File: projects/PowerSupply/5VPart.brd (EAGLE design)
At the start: 50 x 50 mm, 26 parts, among them IC1 LM2596T, IC2 LM2596T, X1 IN, X2 OUT

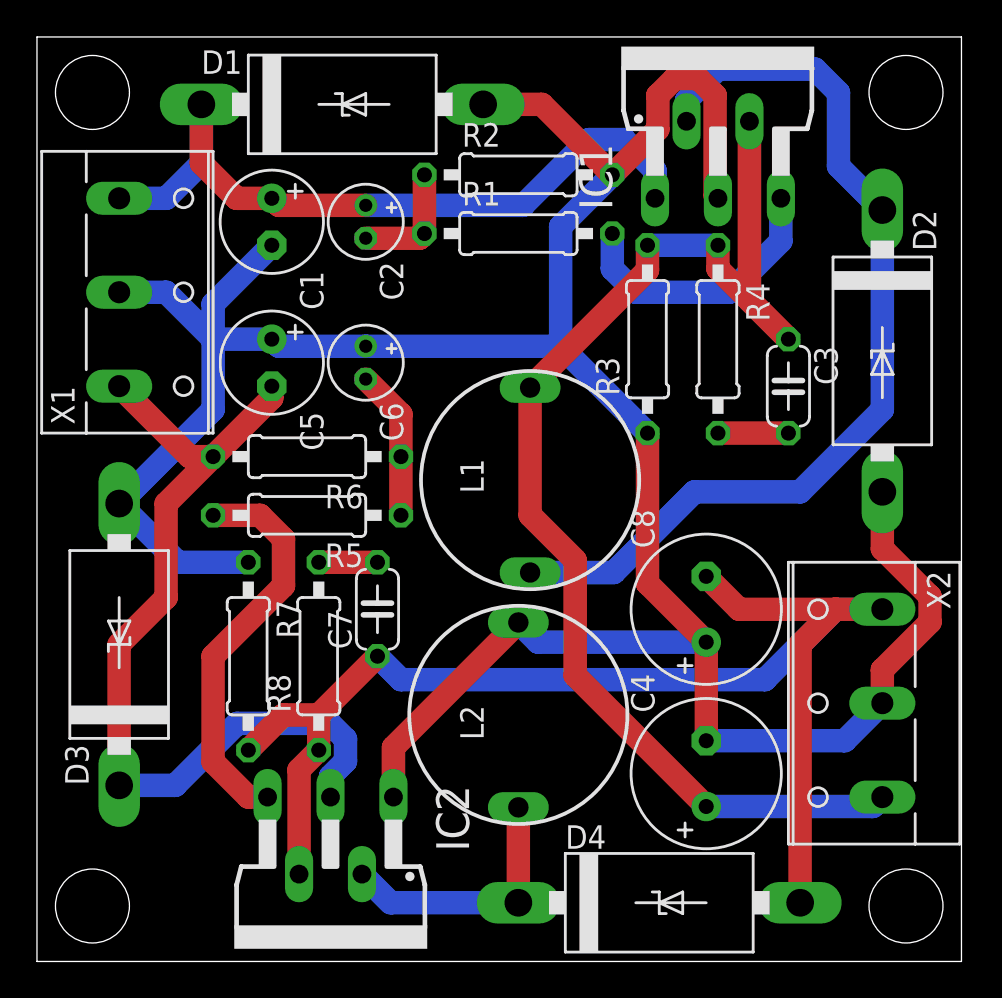
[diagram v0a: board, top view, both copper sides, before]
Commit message: feat: 5v part modified
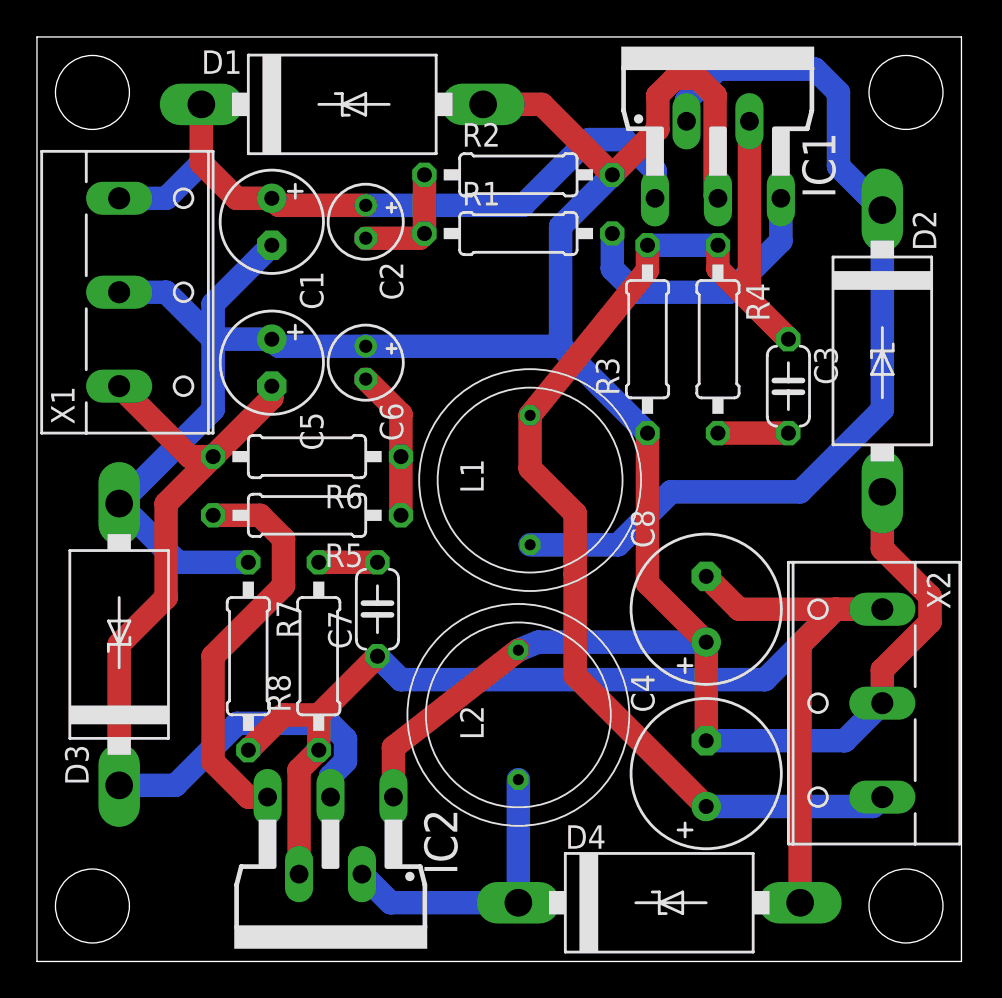
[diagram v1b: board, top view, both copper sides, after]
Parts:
- C8: value 330µF -> 470µF
- L1: device inductor-neosid:SD12-680 -> bb84:IND-120
- L2: value 47µH -> 33µH; device inductor-neosid:SD12-680 -> bb84:IND-120
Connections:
- net +5V: now also L1.P$2; no longer L1.2
- net GND: now also L2.P$2; no longer L2.2
- net N$2: now also L2.P$1; no longer L2.1
- net N$3: now also L1.P$1; no longer L1.1
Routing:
- net N$2: track 14.3 -> 15.8 mm
- net GND: track 155.9 -> 154.6 mm
- net +20V: track 41.4 -> 40.7 mm
- net N$3: track 51.4 -> 50.8 mm
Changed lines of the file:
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@@
 <attribute name="VALUE" x="21.082" y="16.891" size="1.27" layer="27" ratio="10" rot="R90"/>
 </element>
-<element name="C8" library="rcl" library_urn="urn:adsk.eagle:library:334" package="E3,5-8" package3d_urn="urn:adsk.eagle:package:23360/2" value="330µF" x="36.195" y="19.05" smashed="yes" rot="R90">
+<element name="C8" library="rcl" library_urn="urn:adsk.eagle:library:334" package="E3,5-8" package3d_urn="urn:adsk.eagle:package:23360/2" value="470µF" x="36.195" y="19.05" smashed="yes" rot="R90">
 <attribute name="NAME" x="33.401" y="22.352" size="1.27" layer="25" ratio="10" rot="R90"/>
 <attribute name="POPULARITY" value="13" x="66.675" y="49.53" size="1.778" layer="27" rot="R90" display="off"/>
@@
 <attribute name="MF" value="" x="83.82" y="38.735" size="1.778" layer="27" display="off"/>
 <attribute name="MPN" value="LM2596T-ADJ/LF02" x="83.82" y="38.735" size="1.778" layer="27" display="off"/>
-<attribute name="NAME" x="31.115" y="40.64" size="1.778" layer="25" ratio="10" rot="R90"/>
+<attribute name="NAME" x="43.18" y="41.275" size="1.778" layer="25" ratio="10" rot="R90"/>
 <attribute name="OC_FARNELL" value="9494162" x="83.82" y="38.735" size="1.778" layer="27" display="off"/>
 <attribute name="OC_NEWARK" value="65K5910" x="83.82" y="38.735" size="1.778" layer="27" display="off"/>
@@
 <attribute name="MF" value="" x="-5.715" y="24.13" size="1.778" layer="27" rot="R180" display="off"/>
 <attribute name="MPN" value="LM2596T-ADJ/LF02" x="-5.715" y="24.13" size="1.778" layer="27" rot="R180" display="off"/>
-<attribute name="NAME" x="21.59" y="9.525" size="1.778" layer="25" ratio="10" rot="R270"/>
+<attribute name="NAME" x="20.955" y="8.255" size="1.778" layer="25" ratio="10" rot="R270"/>
 <attribute name="OC_FARNELL" value="9494162" x="-5.715" y="24.13" size="1.778" layer="27" rot="R180" display="off"/>
 <attribute name="OC_NEWARK" value="65K5910" x="-5.715" y="24.13" size="1.778" layer="27" rot="R180" display="off"/>
@@
 <attribute name="VALUE" x="1.27" y="5.715" size="1.778" layer="27" ratio="10"/>
 </element>
-<element name="L1" library="inductor-neosid" library_urn="urn:adsk.eagle:library:241" package="SD12-680" package3d_urn="urn:adsk.eagle:package:14657/1" value="33µH" x="26.67" y="26.035" smashed="yes" rot="R90">
-<attribute name="MF" value="BUSSMANN" x="33.02" y="45.085" size="1.778" layer="27" rot="R90" display="off"/>
-<attribute name="MPN" value="SD12-680" x="33.02" y="45.085" size="1.778" layer="27" rot="R90" display="off"/>
+<element name="L1" library="bb84" package="IND-120" value="33µH" x="26.67" y="26.035" smashed="yes" rot="R90">
 <attribute name="NAME" x="24.162" y="25.317" size="1.27" layer="25" rot="R90"/>
-<attribute name="OC_FARNELL" value="unknown" x="33.02" y="45.085" size="1.778" layer="27" rot="R90" display="off"/>
-<attribute name="OC_NEWARK" value="19K7201" x="33.02" y="45.085" size="1.778" layer="27" rot="R90" display="off"/>
-<attribute name="POPULARITY" value="0" x="33.02" y="45.085" size="1.778" layer="27" rot="R90" display="off"/>
 <attribute name="VALUE" x="29.67" y="23.42" size="1.27" layer="27" rot="R90"/>
 </element>
-<element name="L2" library="inductor-neosid" library_urn="urn:adsk.eagle:library:241" package="SD12-680" package3d_urn="urn:adsk.eagle:package:14657/1" value="47µH" x="26.035" y="13.335" smashed="yes" rot="R90">
-<attribute name="MF" value="BUSSMANN" x="32.385" y="45.085" size="1.778" layer="27" rot="R90" display="off"/>
-<attribute name="MPN" value="SD12-680" x="32.385" y="45.085" size="1.778" layer="27" rot="R90" display="off"/>
+<element name="L2" library="bb84" package="IND-120" value="33µH" x="26.035" y="13.335" smashed="yes" rot="R90">
 <attribute name="NAME" x="24.162" y="11.982" size="1.27" layer="25" rot="R90"/>
-<attribute name="OC_FARNELL" value="unknown" x="32.385" y="45.085" size="1.778" layer="27" rot="R90" display="off"/>
-<attribute name="OC_NEWARK" value="19K7201" x="32.385" y="45.085" size="1.778" layer="27" rot="R90" display="off"/>
-<attribute name="POPULARITY" value="0" x="32.385" y="45.085" size="1.778" layer="27" rot="R90" display="off"/>
 <attribute name="VALUE" x="29.035" y="10.72" size="1.27" layer="27" rot="R90"/>
 </element>
@@
 <contactref element="R3" pad="1"/>
 <contactref element="D2" pad="A"/>
-<contactref element="L2" pad="2"/>
+<contactref element="L2" pad="P$2"/>
 <contactref element="R7" pad="1"/>
 <contactref element="C8" pad="+"/>
@@
 <contactref element="X1" pad="2"/>
 <wire x1="19.2786" y1="8.89" x2="19.2786" y2="11.5786" width="1.27" layer="1"/>
-<wire x1="19.2786" y1="11.5786" x2="26.035" y2="18.335" width="1.27" layer="1"/>
+<wire x1="19.2786" y1="11.5786" x2="26.035" y2="16.835" width="1.27" layer="1"/>
 <wire x1="36.195" y1="11.938" x2="36.195" y2="17.272" width="1.27" layer="1"/>
 <wire x1="36.195" y1="17.272" x2="33.02" y2="20.447" width="1.27" layer="1"/>
@@
 <wire x1="43.688" y1="11.938" x2="45.72" y2="13.97" width="1.27" layer="16"/>
 <wire x1="36.195" y1="17.272" x2="27.098" y2="17.272" width="1.27" layer="16"/>
-<wire x1="27.098" y1="17.272" x2="26.035" y2="18.335" width="1.27" layer="16"/>
+<wire x1="27.098" y1="17.272" x2="26.035" y2="16.835" width="1.27" layer="16"/>
 <wire x1="17.78" y1="33.274" x2="28.321" y2="33.274" width="1.27" layer="16"/>
 <wire x1="28.321" y1="33.274" x2="33.02" y2="28.575" width="1.27" layer="16"/>
@@
 <contactref element="IC1" pad="2"/>
 <contactref element="D2" pad="C"/>
-<contactref element="L1" pad="1"/>
-<wire x1="26.67" y1="21.035" x2="31.195" y2="21.035" width="1.27" layer="16"/>
-<wire x1="31.195" y1="21.035" x2="35.56" y2="25.4" width="1.27" layer="16"/>
-<wire x1="35.56" y1="25.4" x2="41.275" y2="25.4" width="1.27" layer="16"/>
-<wire x1="41.275" y1="25.4" x2="45.72" y2="29.845" width="1.27" layer="16"/>
+<contactref element="L1" pad="P$1"/>
+<wire x1="45.72" y1="29.845" x2="41.275" y2="25.4" width="1.27" layer="16"/>
 <wire x1="45.72" y1="29.845" x2="45.72" y2="40.64" width="1.27" layer="16"/>
 <wire x1="45.72" y1="40.64" x2="43.349" y2="43.011" width="1.27" layer="16"/>
@@
 <wire x1="36.83" y1="48.26" x2="35.1282" y2="46.5582" width="1.27" layer="16"/>
 <wire x1="35.1282" y1="46.5582" x2="35.1282" y2="45.4406" width="1.27" layer="16"/>
+<wire x1="31.425" y1="22.535" x2="26.67" y2="22.535" width="1.27" layer="16"/>
+<wire x1="41.275" y1="25.4" x2="34.29" y2="25.4" width="1.27" layer="16"/>
+<wire x1="34.29" y1="25.4" x2="31.425" y2="22.535" width="1.27" layer="16"/>
 </signal>
 <signal name="N$2">
-<contactref element="L2" pad="1"/>
+<contactref element="L2" pad="P$1"/>
 <contactref element="IC2" pad="2"/>
 <contactref element="D4" pad="C"/>
-<wire x1="26.035" y1="3.175" x2="26.035" y2="8.335" width="1.27" layer="1"/>
 <wire x1="26.035" y1="3.175" x2="19.1262" y2="3.175" width="1.27" layer="16"/>
 <wire x1="19.1262" y1="3.175" x2="17.5768" y2="4.7244" width="1.27" layer="16"/>
+<wire x1="26.035" y1="3.175" x2="26.035" y2="9.835" width="1.27" layer="16"/>
 </signal>
 <signal name="N$5">
@@
 <contactref element="R4" pad="1"/>
 <contactref element="C3" pad="1"/>
-<contactref element="L1" pad="2"/>
+<contactref element="L1" pad="P$2"/>
 <contactref element="C4" pad="+"/>
 <wire x1="40.64" y1="33.655" x2="36.83" y2="37.465" width="1.27" layer="1"/>
@@
 <wire x1="38.5318" y1="35.7632" x2="40.64" y2="33.655" width="1.27" layer="1"/>
 <wire x1="33.02" y1="38.735" x2="33.02" y2="37.385" width="1.27" layer="1"/>
-<wire x1="33.02" y1="37.385" x2="26.67" y2="31.035" width="1.27" layer="1"/>
-<wire x1="26.67" y1="31.035" x2="26.67" y2="24.14028125" width="1.27" layer="1"/>
-<wire x1="26.67" y1="24.14028125" x2="29.1074" y2="21.70288125" width="1.27" layer="1"/>
+<wire x1="33.02" y1="37.385" x2="26.67" y2="29.535" width="1.27" layer="1"/>
 <wire x1="29.1074" y1="15.4696" x2="36.195" y2="8.382" width="1.27" layer="1"/>
-<wire x1="29.1074" y1="21.70288125" x2="29.1074" y2="15.4696" width="1.27" layer="1"/>
+<wire x1="29.1074" y1="21.70288125" x2="29.1074" y2="20.955" width="1.27" layer="1"/>
+<wire x1="29.1074" y1="20.955" x2="29.1074" y2="15.4696" width="1.27" layer="1"/>
 <wire x1="33.02" y1="38.735" x2="36.83" y2="38.735" width="1.27" layer="16"/>
 <contactref element="X2" pad="1"/>
 <wire x1="45.72" y1="8.89" x2="45.212" y2="8.382" width="1.27" layer="16"/>
 <wire x1="45.212" y1="8.382" x2="36.195" y2="8.382" width="1.27" layer="16"/>
+<wire x1="26.67" y1="29.535" x2="26.67" y2="26.67" width="1.27" layer="1"/>
+<wire x1="29.1074" y1="24.2326" x2="29.1074" y2="21.70288125" width="1.27" layer="1"/>
+<wire x1="26.67" y1="26.67" x2="29.1074" y2="24.2326" width="1.27" layer="1"/>
 </signal>
 <signal name="-5V">
@@
 <contactref element="C2" pad="+"/>
 <contactref element="D1" pad="C"/>
-<wire x1="8.89" y1="45.72" x2="8.89" y2="46.355" width="1.27" layer="1"/>
-<wire x1="8.89" y1="43.18" x2="10.795" y2="41.275" width="1.27" layer="1"/>
+<wire x1="10.795" y1="41.275" x2="8.89" y2="43.18" width="1.27" layer="1"/>
 <wire x1="10.795" y1="41.275" x2="12.7" y2="41.275" width="1.27" layer="1"/>
-<wire x1="8.89" y1="46.355" x2="8.89" y2="43.18" width="1.27" layer="1"/>
 <wire x1="17.78" y1="40.894" x2="13.081" y2="40.894" width="1.27" layer="1"/>
 <wire x1="13.081" y1="40.894" x2="12.7" y2="41.275" width="1.27" layer="1"/>
@@
 <wire x1="8.89" y1="43.18" x2="6.985" y2="41.275" width="1.27" layer="16"/>
 <wire x1="6.985" y1="41.275" x2="4.445" y2="41.275" width="1.27" layer="16"/>
+<wire x1="8.89" y1="43.18" x2="8.89" y2="46.355" width="1.27" layer="1"/>
 </signal>
 <signal name="-20V">

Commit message: feat: 5 volt part modified
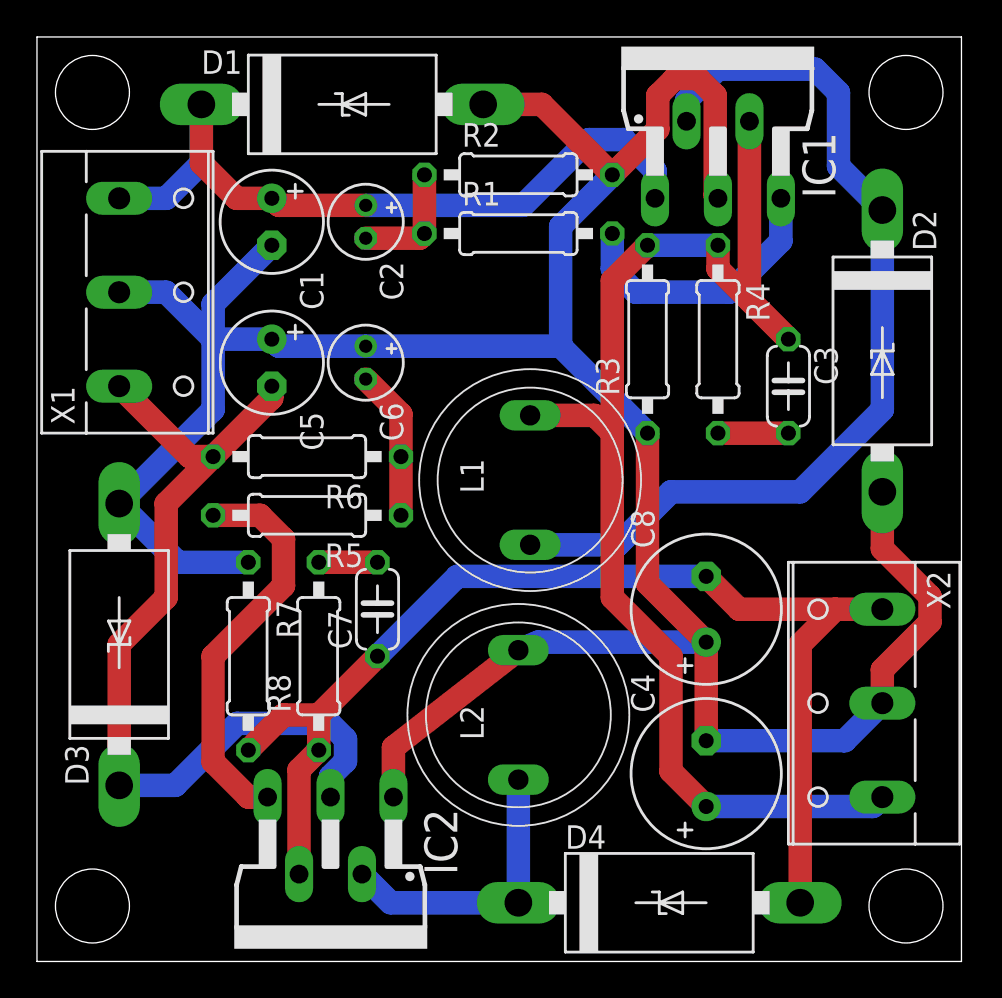
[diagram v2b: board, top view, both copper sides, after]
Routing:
- net -5V: track 74.5 -> 64.6 mm
- net +5V: track 69.4 -> 71.0 mm
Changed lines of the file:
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@@
 <wire x1="38.5318" y1="45.4406" x2="38.5318" y2="35.7632" width="1.27" layer="1"/>
 <wire x1="38.5318" y1="35.7632" x2="40.64" y2="33.655" width="1.27" layer="1"/>
-<wire x1="33.02" y1="38.735" x2="33.02" y2="37.385" width="1.27" layer="1"/>
-<wire x1="33.02" y1="37.385" x2="26.67" y2="29.535" width="1.27" layer="1"/>
-<wire x1="29.1074" y1="15.4696" x2="36.195" y2="8.382" width="1.27" layer="1"/>
-<wire x1="29.1074" y1="21.70288125" x2="29.1074" y2="20.955" width="1.27" layer="1"/>
-<wire x1="29.1074" y1="20.955" x2="29.1074" y2="15.4696" width="1.27" layer="1"/>
 <wire x1="33.02" y1="38.735" x2="36.83" y2="38.735" width="1.27" layer="16"/>
 <contactref element="X2" pad="1"/>
 <wire x1="45.72" y1="8.89" x2="45.212" y2="8.382" width="1.27" layer="16"/>
 <wire x1="45.212" y1="8.382" x2="36.195" y2="8.382" width="1.27" layer="16"/>
-<wire x1="26.67" y1="29.535" x2="26.67" y2="26.67" width="1.27" layer="1"/>
-<wire x1="29.1074" y1="24.2326" x2="29.1074" y2="21.70288125" width="1.27" layer="1"/>
-<wire x1="26.67" y1="26.67" x2="29.1074" y2="24.2326" width="1.27" layer="1"/>
+<wire x1="36.195" y1="8.382" x2="34.29" y2="10.287" width="1.27" layer="1"/>
+<wire x1="34.29" y1="10.287" x2="34.29" y2="16.51" width="1.27" layer="1"/>
+<wire x1="34.29" y1="16.51" x2="31.115" y2="19.685" width="1.27" layer="1"/>
+<wire x1="31.115" y1="19.685" x2="31.115" y2="28.575" width="1.27" layer="1"/>
+<wire x1="30.155" y1="29.535" x2="31.115" y2="28.575" width="1.27" layer="1"/>
+<wire x1="30.155" y1="29.535" x2="26.67" y2="29.535" width="1.27" layer="1"/>
+<wire x1="31.115" y1="28.575" x2="31.115" y2="36.83" width="1.27" layer="1"/>
+<wire x1="31.115" y1="36.83" x2="33.02" y2="38.735" width="1.27" layer="1"/>
 </signal>
 <signal name="-5V">
@@
 <wire x1="15.24" y1="13.335" x2="18.415" y2="16.51" width="1.27" layer="1"/>
 <contactref element="X2" pad="3"/>
-<wire x1="39.37" y1="15.24" x2="19.685" y2="15.24" width="1.27" layer="16"/>
 <wire x1="37.973" y1="19.05" x2="43.18" y2="19.05" width="1.27" layer="1"/>
 <wire x1="43.18" y1="19.05" x2="45.72" y2="19.05" width="1.27" layer="1"/>
 <wire x1="41.275" y1="17.145" x2="43.18" y2="19.05" width="1.27" layer="1"/>
-<wire x1="39.37" y1="15.24" x2="43.18" y2="19.05" width="1.27" layer="16"/>
-<wire x1="43.18" y1="19.05" x2="45.72" y2="19.05" width="1.27" layer="16"/>
 <wire x1="36.195" y1="20.828" x2="37.973" y2="19.05" width="1.27" layer="1"/>
 <wire x1="41.275" y1="3.175" x2="41.275" y2="17.145" width="1.27" layer="1"/>
-<wire x1="19.685" y1="15.24" x2="18.415" y2="16.51" width="1.27" layer="16"/>
 <wire x1="11.43" y1="11.43" x2="13.335" y2="13.335" width="1.27" layer="1"/>
 <wire x1="13.335" y1="13.335" x2="15.24" y2="13.335" width="1.27" layer="1"/>
+<wire x1="18.415" y1="16.51" x2="22.733" y2="20.828" width="1.27" layer="16"/>
+<wire x1="22.733" y1="20.828" x2="36.195" y2="20.828" width="1.27" layer="16"/>
 </signal>
 <signal name="+20V">
